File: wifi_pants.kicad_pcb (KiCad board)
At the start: 2 copper layers, 65 x 30 mm, 126 parts, among them P1 CONN_02X20, P2 POWER / UART, P3 JST PH POWER IN, U1 ESP-12E, U2 TPS6123x

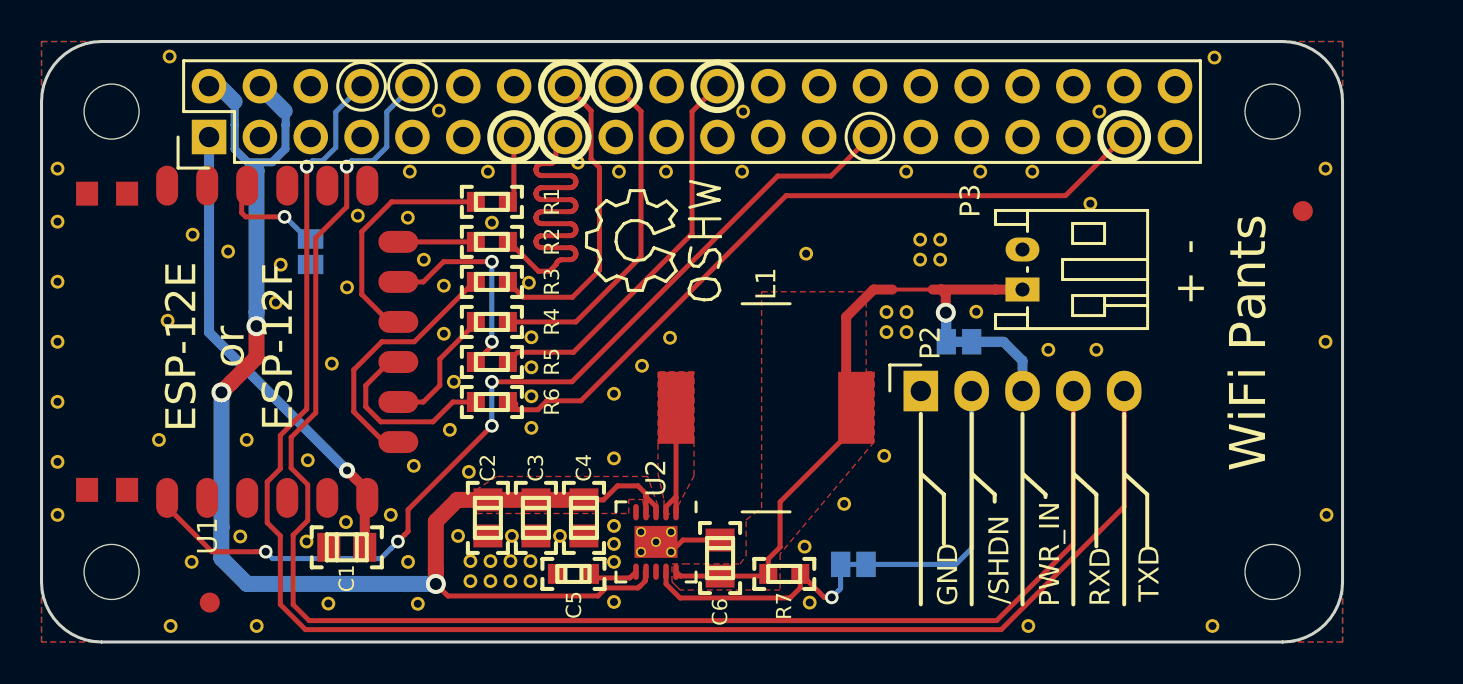
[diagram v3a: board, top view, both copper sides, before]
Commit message: Add UVLO for LiPo, rearrange boost layout, make PWR_IN on header disconnected by default
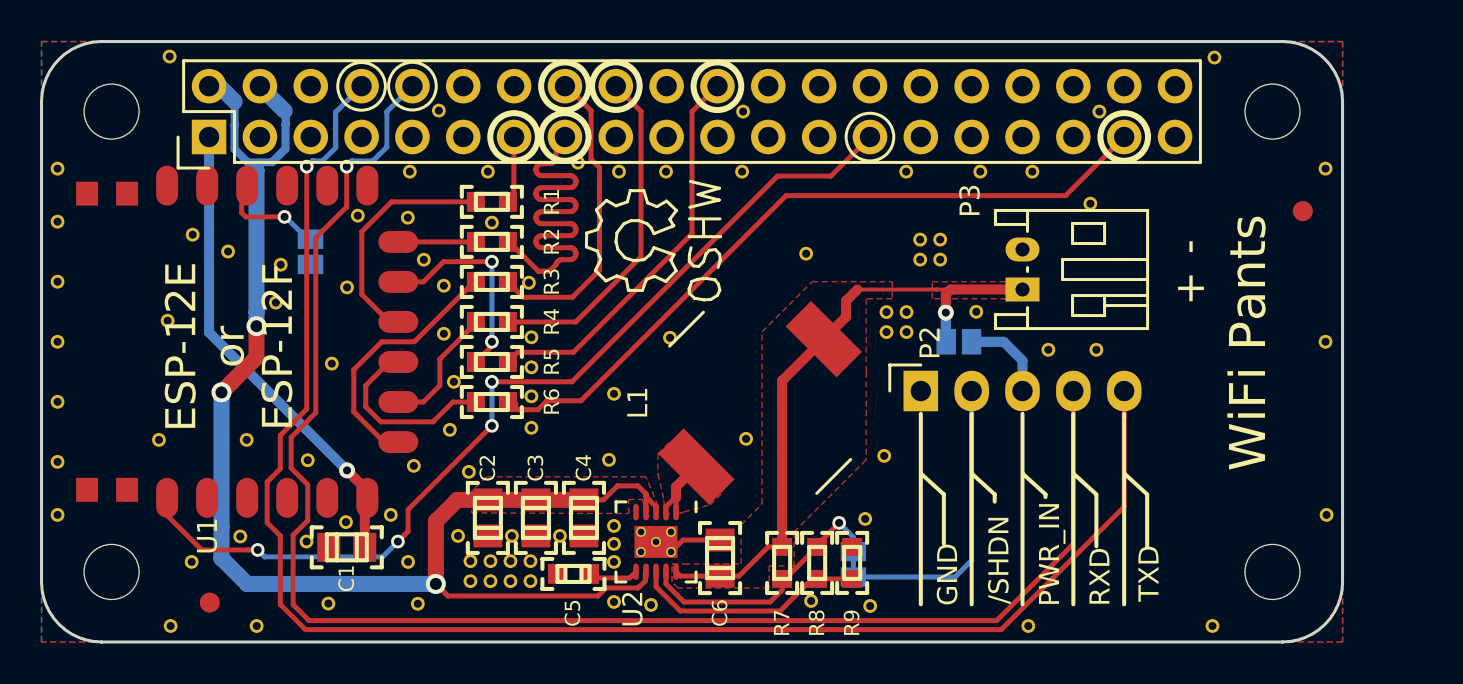
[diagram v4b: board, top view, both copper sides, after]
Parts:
- removed the REF**1 at (103.4, 113.0)
- removed the REF**6 at (103.1, 110.2)
- added R8: 33K 1%, mcous:0603(1608m)-CHIP-RESISTOR, F.Cu at (103.8, 111.0)
- added R9: 1K 1%, mcous:0603(1608m)-CHIP-RESISTOR, F.Cu at (105.5, 111.0)
- added REF**1: VIA_0.40mm, wifi_pants:VIA_0.40mm, F.Cu at (95.5, 113.2)
- added REF**1: VIA_0.40mm, wifi_pants:VIA_0.40mm, F.Cu at (106.4, 113.2)
- added REF**1: VIA_0.40mm, wifi_pants:VIA_0.40mm, F.Cu at (103.5, 113.0)
- R7: value 22K -> 47K 1%
- moved REF** 6.35 mm to (100.2, 104.8)
- moved REF**6 1.29 mm to (106.2, 108.8)
- moved R7 0.56 mm to (102.0, 111.0), turned to 270 degrees
- moved L1 0.39 mm to (100.9, 103.0), turned to 225 degrees
- moved REF** 0.26 mm to (93.3, 105.9)
- turned JP1 to 180 degrees
- turned JP2 to 270 degrees
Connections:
- JP2 pad 2: PWR_IN -> Net-(JP2-Pad2)
- P2 pad 3: PWR_IN -> Net-(JP2-Pad2)
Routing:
- net Net-(R8-Pad2): track 0.00 -> 11.8 mm
- net PWR_IN: track 37.7 -> 31.3 mm
- net Net-(JP2-Pad2): track 0.00 -> 4.45 mm
- net Net-(L1-Pad2): track 5.89 -> 3.38 mm
- net /SHDN: track 27.1 -> 29.6 mm
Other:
- board text added: "r4"
- board text removed: "r3"

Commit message: logo and serial number added
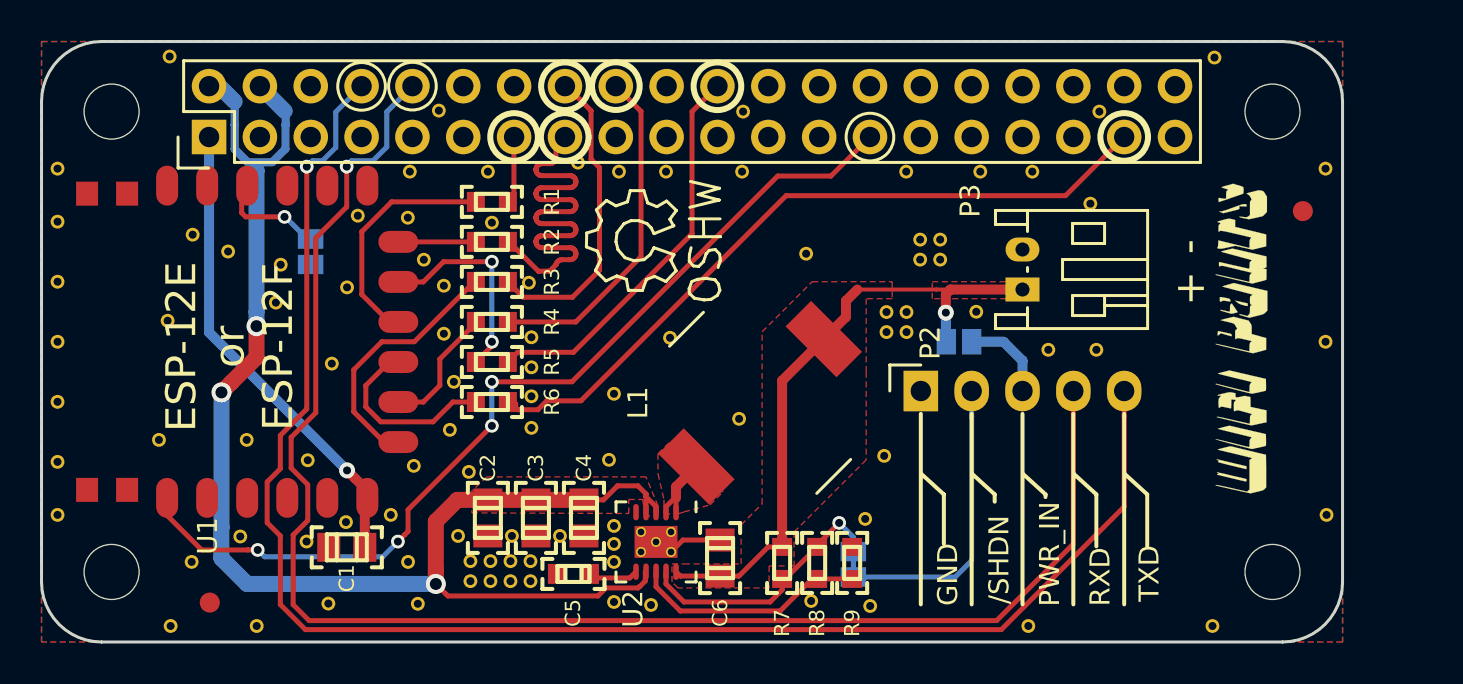
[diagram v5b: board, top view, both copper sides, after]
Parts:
- added G***: LOGO, wifi_pants:wifi_pants_logo, F.Cu at (125.0, 99.8)
- added G***: LOGO, wifi_pants:wifi_pants_logo, B.Cu at (122.3, 100.0)
- added G***: LOGO, wifi_pants:snbox, B.Cu at (70.5, 100.0)
- moved REF** 1.06 mm to (99.8, 103.8)
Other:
- board text added: "r4 3/20/16"
- board text removed: "WiFi Pants"
- board text removed: "r4"
